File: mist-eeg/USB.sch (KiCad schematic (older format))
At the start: 33 parts, among them J2 USB_C_Receptacle, U3 SST25VF010A, U4 TPS65987DDJ

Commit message: Hooked-up the SoM
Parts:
- renumbered TP2 to TP3
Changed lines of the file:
@@
 Connection ~ 3450 4750
 $Comp
-L Connector:TestPoint TP2
+L Connector:TestPoint TP3
 U 1 1 60D7961B
 P 3350 4650
-F 0 "TP2" H 3292 4768 50  0000 R CNN
+F 0 "TP3" H 3292 4768 50  0000 R CNN
 F 1 "USB_RST" H 3292 4677 50  0000 R CNN
 F 2 "TestPoint:TestPoint_Pad_D1.0mm" H 3550 4650 50  0001 C CNN

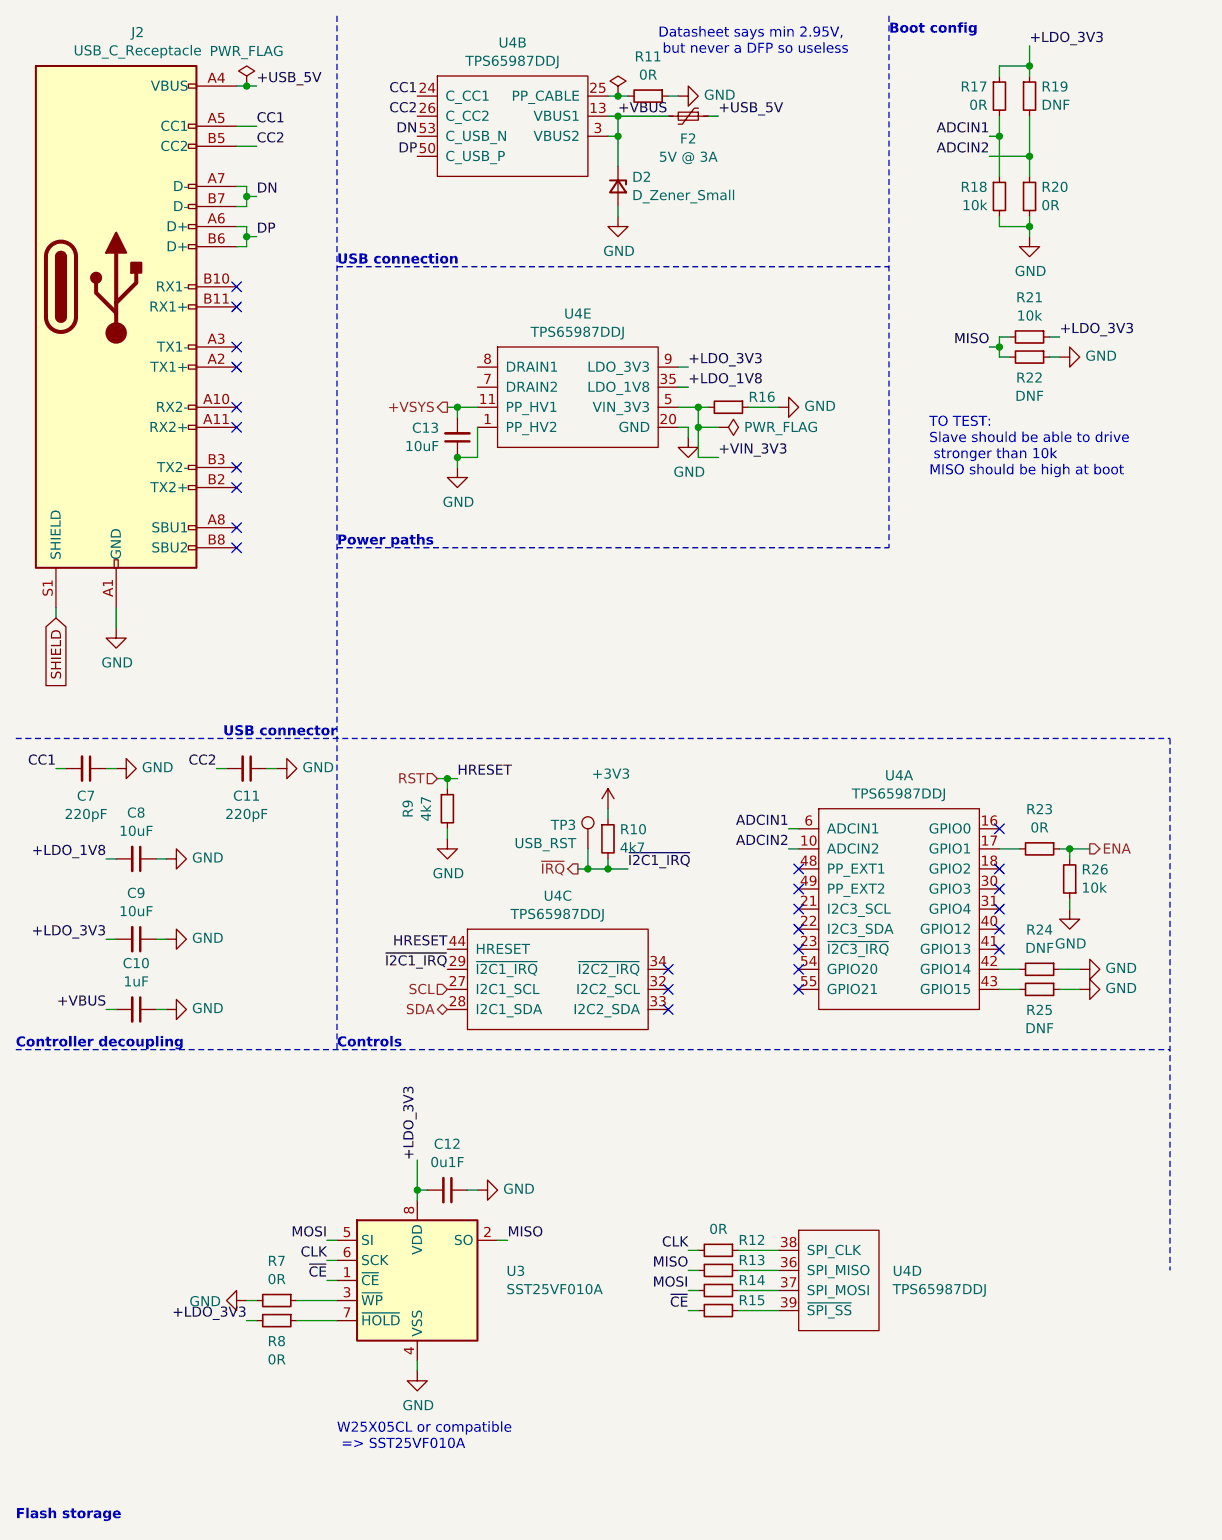
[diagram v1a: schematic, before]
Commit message: Finish schematic and create interface specifications
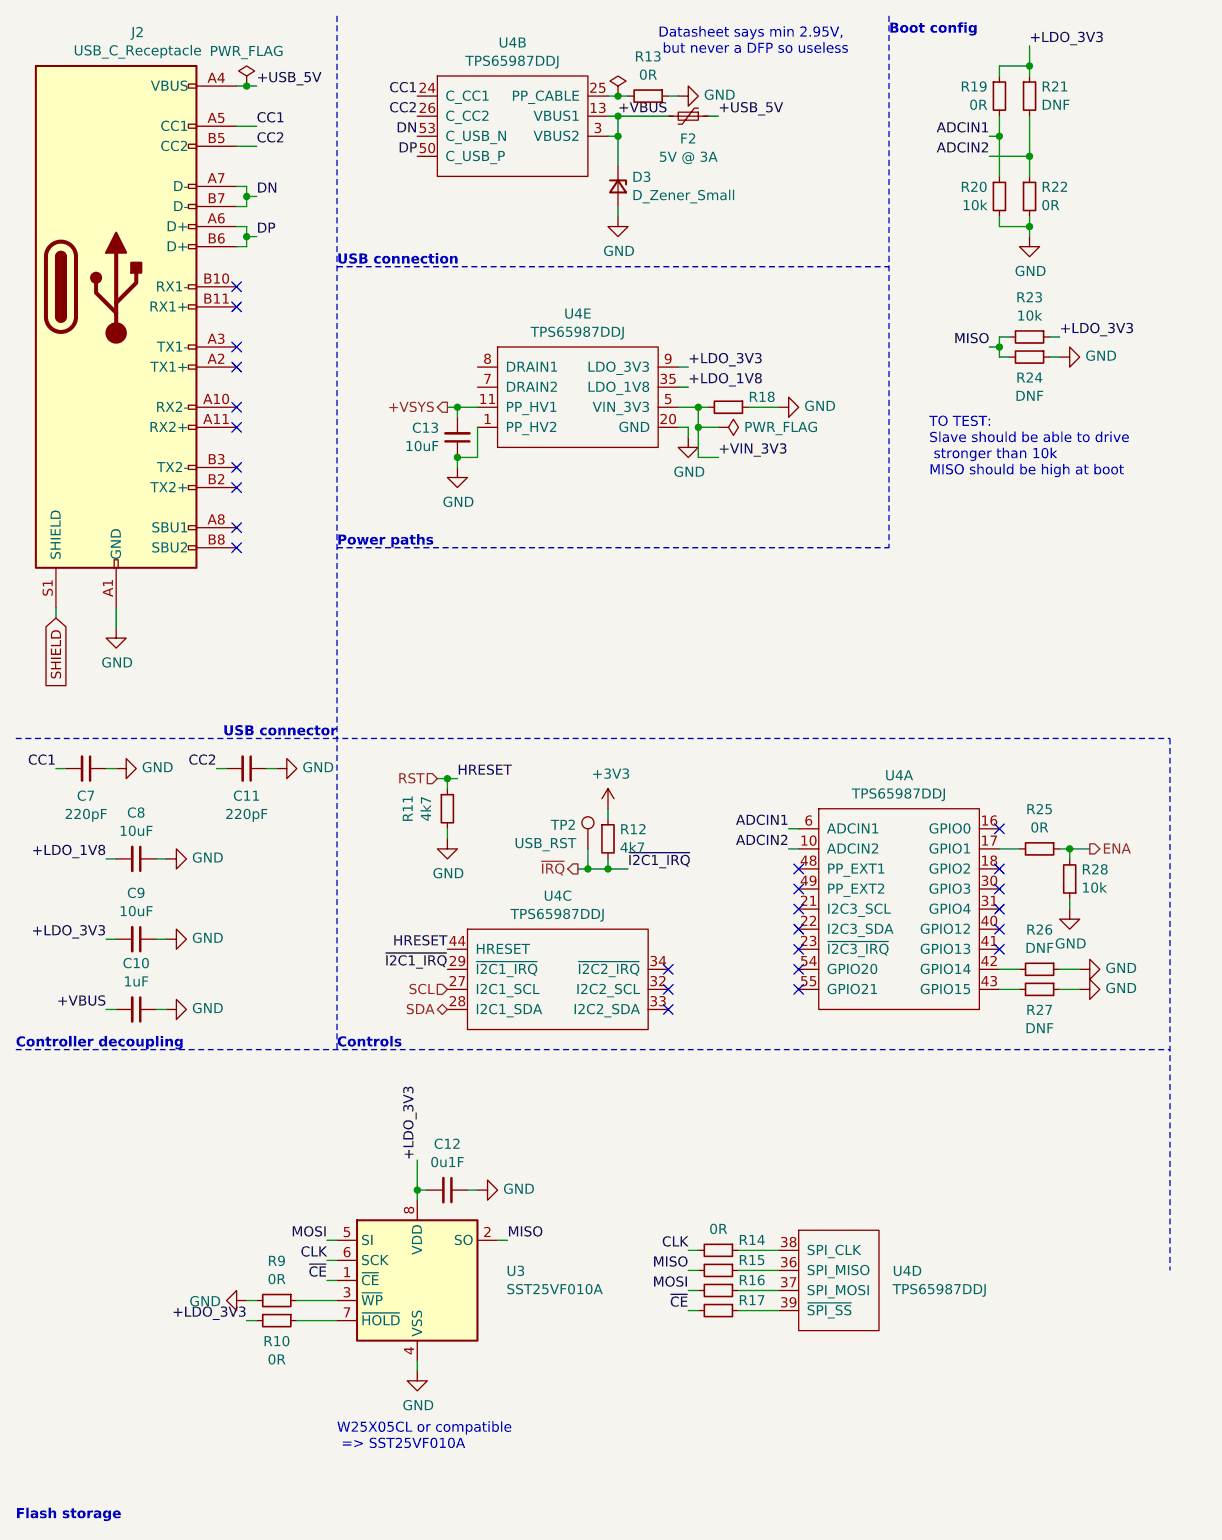
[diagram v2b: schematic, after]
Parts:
- J2: footprint (none) -> Connector_USB:USB_C_Receptacle_Amphenol_12401610E4-2A
- renumbered D2 to D3, R8 to R10, R9 to R11, R10 to R12, R11 to R13, R12 to R14, R13 to R15, R14 to R16, R15 to R17, R16 to R18, R17 to R19, R18 to R20, R19 to R21, R20 to R22, R21 to R23, R22 to R24, R23 to R25, R24 to R26, R25 to R27, R26 to R28, R7 to R9, TP3 to TP2
